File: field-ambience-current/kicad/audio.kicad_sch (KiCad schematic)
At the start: 29 parts, among them J6 Speaker L header (2-pin, to S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, J7 Speaker R header (2-pin, to S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, J8 3.5mm TRS Line/Headphone Out 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, U3 PCM5102A I²S DAC (TSSOP-20), U4 PAM8403H Class-D Stereo Amp (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

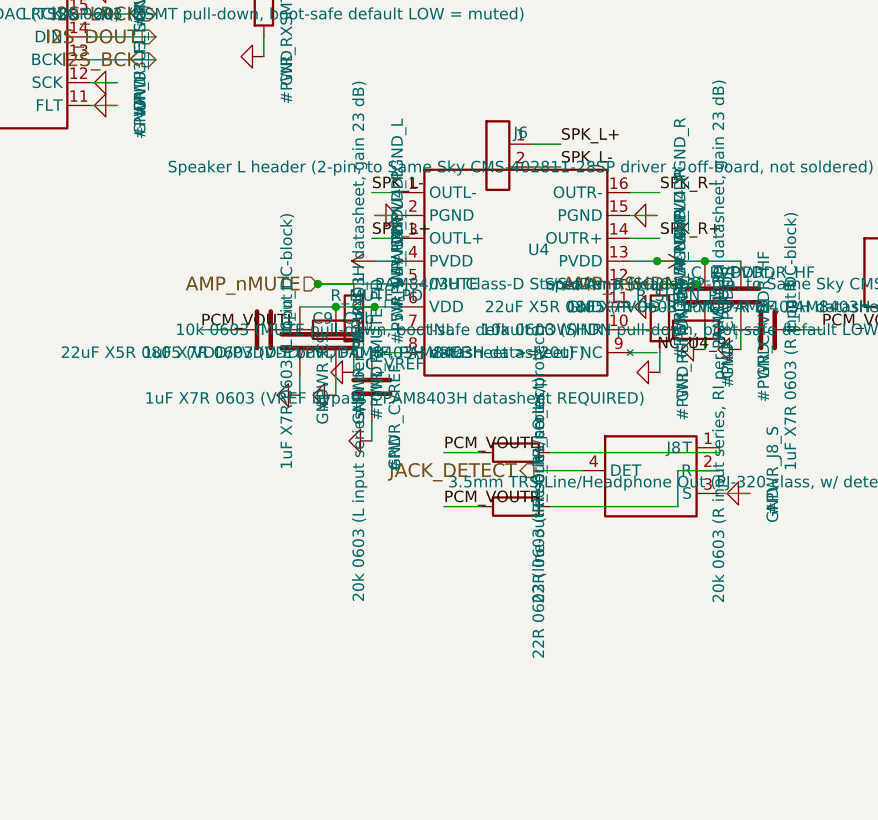
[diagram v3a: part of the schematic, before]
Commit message: fix(pcb): datasheet verification of all remaining parts — encoder + jack pad maps were dead/wrong (r18.82) (#94)
User asked to verify all other components against datasheets. Every
remaining IC and every symbol-pin<->footprint-pad pairing was checked
against the official documents (Microchip DS20001952 + DS20001984, NXP
PCA9685 Rev 4, ST USBLC6-2 + DS12110 Fig 5, Abracon via LCSC, SHOU HAN
PJ-320D, HX B3F-4055, KiCad footprint sources).

Critical pad-mapping bugs (KiCad matches pin number to pad name as a
STRING):

1. All 4 rotary encoders were completely unconnected: the official KiCad
   footprint RotaryEncoder_Alps_EC11E-Switch_Vertical_H20mm uses NAMED
   pads A/B/C/S1/S2, the custom symbol used numeric pins 1-5 - not a
   single encoder pin would have joined a pad in the netlist. Symbol pin
   numbers renamed to the pad names (footprint geometry verified from
   the KiCad GitLab source: A(0,0), C(0,2.5) = middle common, B(0,5) =
   ALPS A-C-B terminal order).

2. PJ-320D jacks (J8 line-out, J10 MIDI): pad map was wrong. The SHOU HAN
   drawing (PCB layout + schematic) assigns pad 1=A=sleeve, 2=D=ring,
   3=C=tip-switch(detect), 4=B=tip. The symbol mapped T=1/R=2/S=3/DET=4,
   which put LEFT AUDIO on the grounded sleeve barrel, GND on the detect
   contact and JACK_DETECT on the tip. Corrected to T=4/R=2/S=1/DET=3.
   Vendored footprint geometry matches the drawing exactly (3.0/4.0mm
   pad pitch, 1.0mm locators at 7.0mm) - closes TODO B0b.

3. Consequence of the true detect topology (detect rests on the TIP when
   unplugged, i.e. on the DAC L output at +-3Vpk): added R_DET_J8 10k
   (limits MCP input-clamp current to <300uA - unprotected it would have
   clamped negative half-waves through 22R at >100mA, distorting the
   speaker feed) and C_DET_J8 1uF (filters audio AC off GPA6, fc ~16Hz).
   Levels: unplugged ~0.3V LOW, plugged 3.3V HIGH.

Datasheet-required gaps:

4. MCP73831 was missing the 4.7uF VDD input capacitor from the DS typical
   application - the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
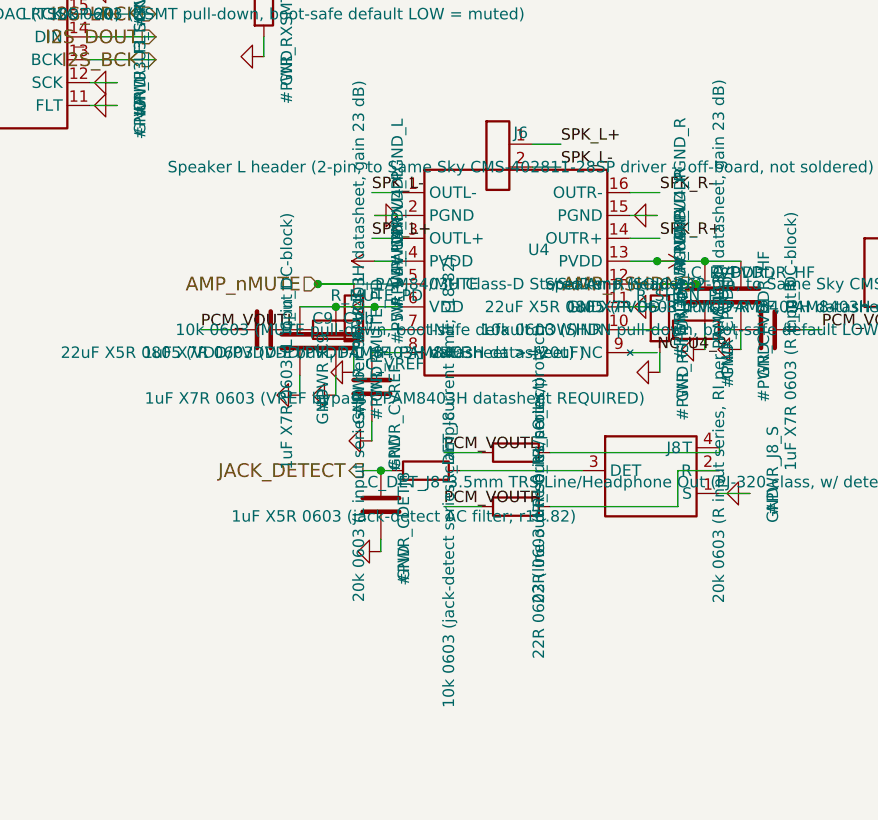
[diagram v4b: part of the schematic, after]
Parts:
- added C_DET_J8: 1uF X5R 0603 (jack-detect AC filter; r18.82), Capacitor_SMD:C_0603_1608Metric, symbol Device:C
- added R_DET_J8: 10k 0603 (jack-detect series, clamp-current limit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, Resistor_SMD:R_0603_1608Metric, symbol Device:R
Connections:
- net GND: now also J8.1 (S), C_DET_J8.2; no longer J8.3 (S)
- net JACK_DETECT: now also C_DET_J8.1, R_DET_J8.1; no longer J8.4 (DET)
- net at R_LO_L.2: now also J8.4 (T); no longer J8.1 (T)
- new net: J8.3 (DET), R_DET_J8.2
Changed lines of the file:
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@@
       (project "field_ambience"
         (path "/66fcdc89-be06-4d61-a855-abf9641d963c" (reference "#PWR_J8_S") (unit 1)))))
+  (symbol (lib_id "Device:R") (at 150 152 90) (unit 1)
+    (in_bom yes) (on_board yes) (dnp no)
+      (property "Reference" "R_DET_J8" (at 152.54 149.46 0)
+        (effects (font (size 1.27 1.27))))
+      (property "Value" "10k 0603 (jack-detect series, clamp-current limit; r18.82)" (at 152.54 153.27 0)
+        (effects (font (size 1.27 1.27))))
+      (property "Footprint" "Resistor_SMD:R_0603_1608Metric" (at 150 152 0)
+        (effects (font (size 1.27 1.27)) hide))
+      (property "Datasheet" "~" (at 150 152 0)
+        (effects (font (size 1.27 1.27)) hide))
+      (property "MPN" "0603WAF1002T5E" (at 152.54 155.81 0)
+        (effects (font (size 1.27 1.27)) hide))
+      (property "LCSC" "C25804" (at 152.54 157.08 0)
+        (effects (font (size 1.27 1.27)) hide))
+    (instances
+      (project "field_ambience"
+        (path "/66fcdc89-be06-4d61-a855-abf9641d963c" (reference "R_DET_J8") (unit 1)))))
+  (symbol (lib_id "Device:C") (at 145 155.81 0) (unit 1)
+    (in_bom yes) (on_board yes) (dnp no)
+      (property "Reference" "C_DET_J8" (at 147.54 153.27 0)
+        (effects (font (size 1.27 1.27))))
+      (property "Value" "1uF X5R 0603 (jack-detect AC filter; r18.82)" (at 147.54 157.08 0)
+        (effects (font (size 1.27 1.27))))
+      (property "Footprint" "Capacitor_SMD:C_0603_1608Metric" (at 145 155.81 0)
+        (effects (font (size 1.27 1.27)) hide))
+      (property "Datasheet" "~" (at 145 155.81 0)
+        (effects (font (size 1.27 1.27)) hide))
+      (property "MPN" "CL10A105KB8NNNC" (at 147.54 159.62 0)
+        (effects (font (size 1.27 1.27)) hide))
+      (property "LCSC" "C15849" (at 147.54 160.89000000000001 0)
+        (effects (font (size 1.27 1.27)) hide))
+    (instances
+      (project "field_ambience"
+        (path "/66fcdc89-be06-4d61-a855-abf9641d963c" (reference "C_DET_J8") (unit 1)))))
+  (symbol (lib_id "Power:GND") (at 145 161 270) (unit 1)
+    (in_bom yes) (on_board yes) (dnp no)
+      (property "Reference" "#PWR_CDETJ8" (at 147.54 158.46 0)
+        (effects (font (size 1.27 1.27))))
+      (property "Value" "GND" (at 147.54 162.27 0)
+        (effects (font (size 1.27 1.27))))
+      (property "Footprint" "" (at 145 161 0)
+        (effects (font (size 1.27 1.27)) hide))
+      (property "Datasheet" "~" (at 145 161 0)
+        (effects (font (size 1.27 1.27)) hide))
+    (instances
+      (project "field_ambience"
+        (path "/66fcdc89-be06-4d61-a855-abf9641d963c" (reference "#PWR_CDETJ8") (unit 1)))))
   (wire (pts (xy 87.3 88.57) (xy 84.3 88.57))
     (stroke (width 0) (type default))
@@
     (stroke (width 0) (type default))
 )
-  (wire (pts (xy 167.38 152) (xy 162 152))
+  (wire (pts (xy 167.38 152) (xy 153.81 152))
+    (stroke (width 0) (type default))
+)
+  (wire (pts (xy 146.19 152) (xy 143 152))
+    (stroke (width 0) (type default))
+)
+  (wire (pts (xy 145 159.62) (xy 145 161))
     (stroke (width 0) (type default))
 )
@@
   (junction (at 181 128.73) (diameter 0) (color 0 0 0 0)
 )
+  (junction (at 145 152) (diameter 0) (color 0 0 0 0)
+)
   (label "PCM_VOUTL" (at 80 101.27 0) (fields_autoplaced)
     (effects (font (size 1.27 1.27)) (justify left bottom))
@@
     (effects (font (size 1.524 1.524)) (justify right))
 )
-  (hierarchical_label "JACK_DETECT" (shape output) (at 162 152 0)
-    (effects (font (size 1.524 1.524)) (justify right))
-)
+  (hierarchical_label "JACK_DETECT" (shape output) (at 143 152 0)
+    (effects (font (size 1.524 1.524)) (justify right))
+)
